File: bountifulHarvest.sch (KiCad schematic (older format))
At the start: 0 parts

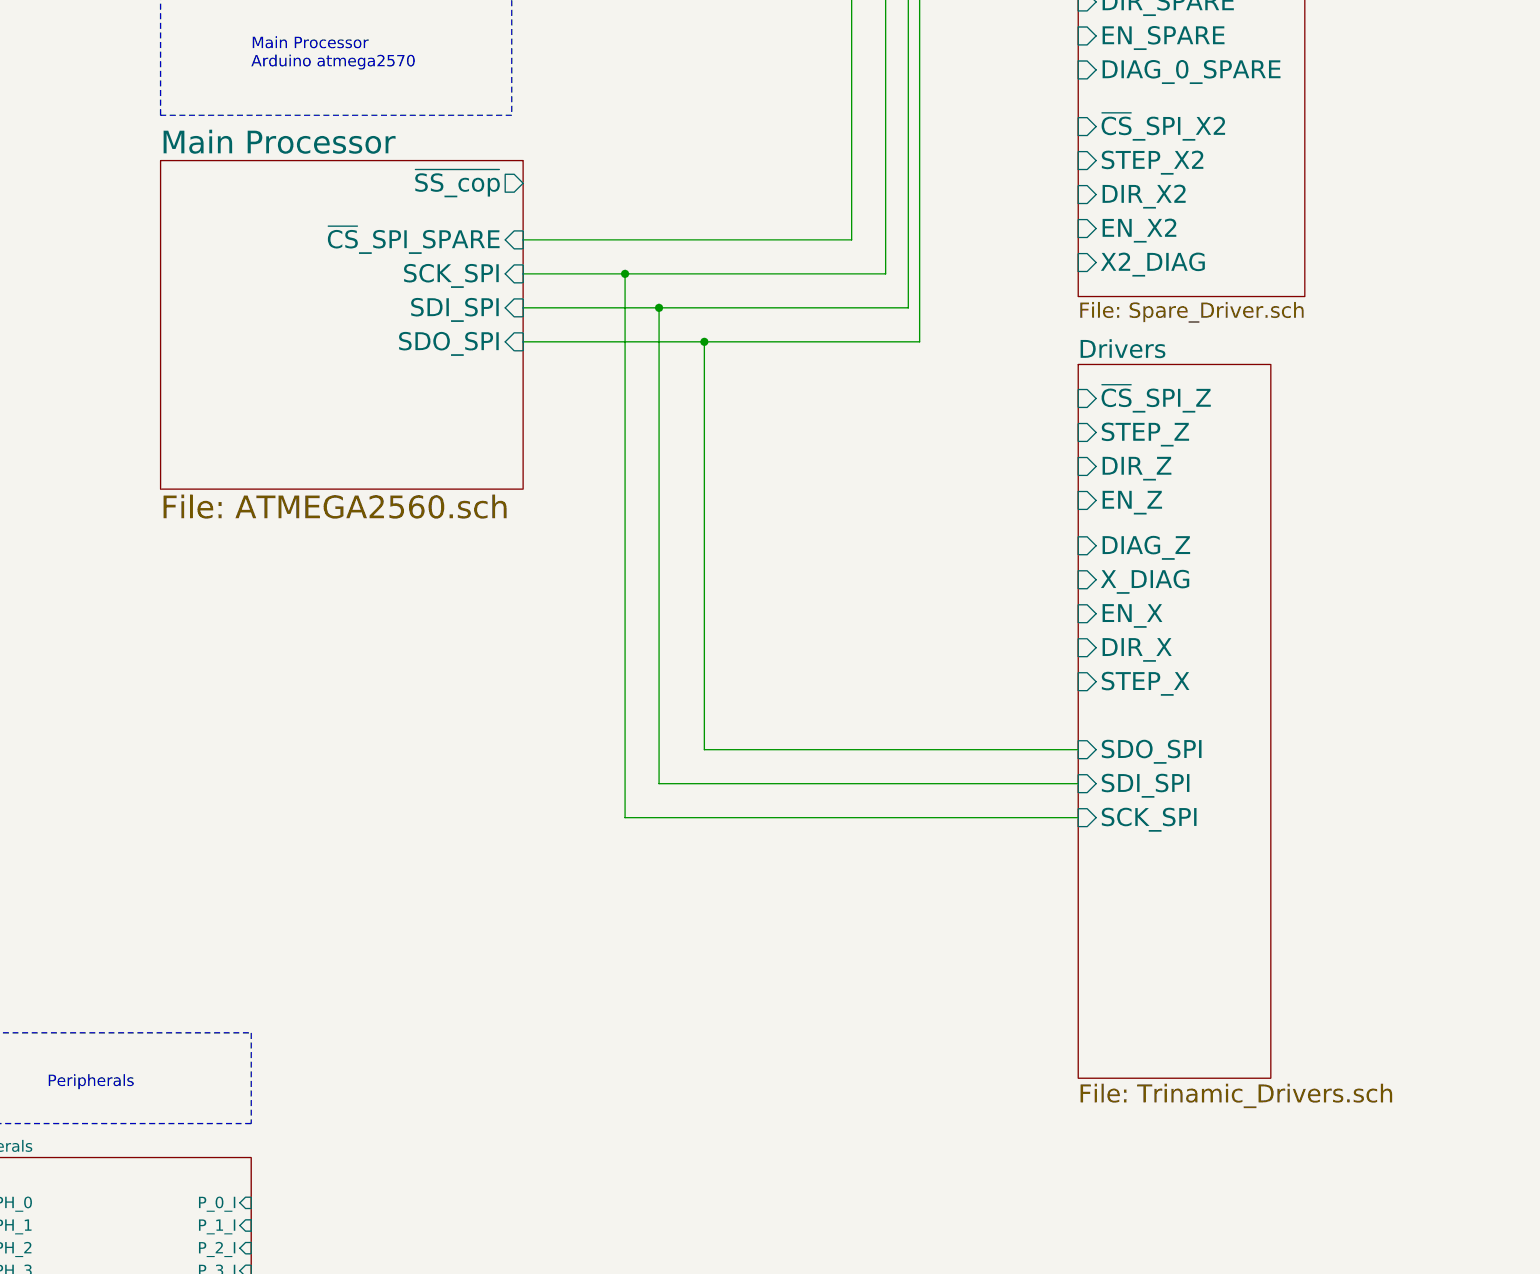
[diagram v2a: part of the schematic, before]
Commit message: Updated bus connections between drivers at ATMega
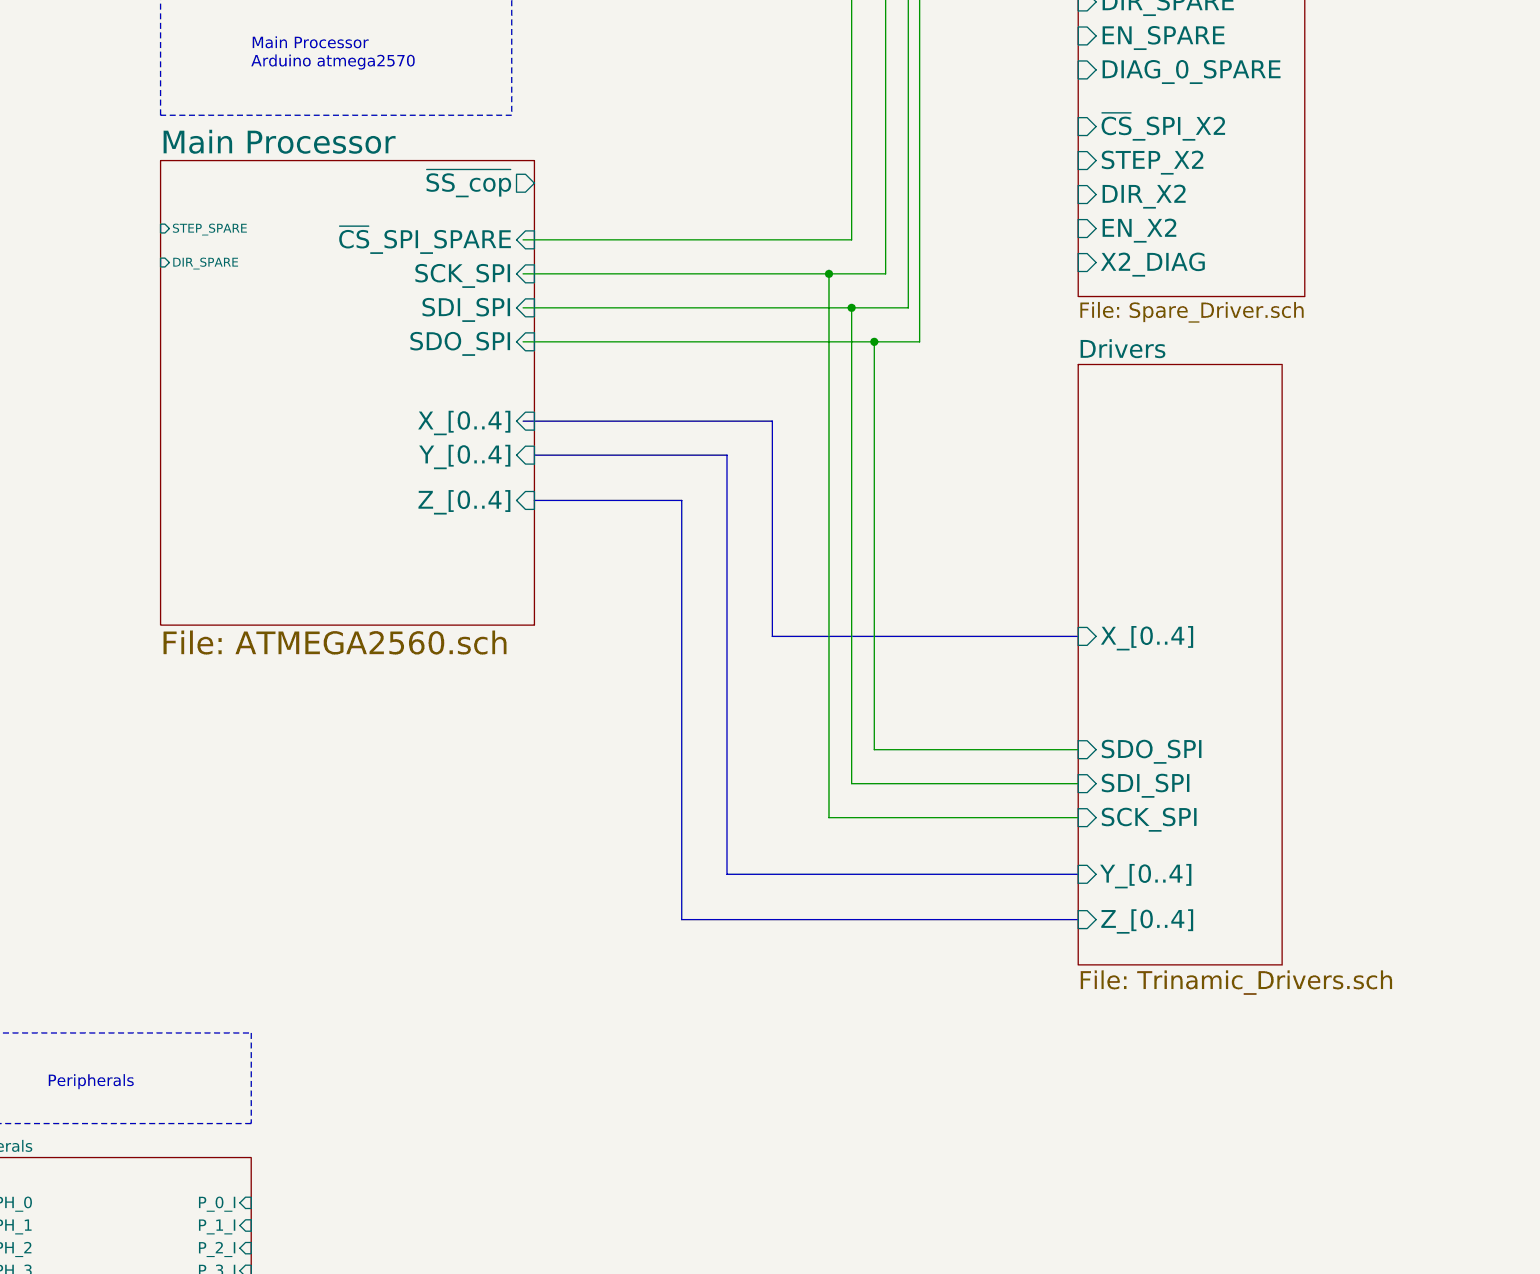
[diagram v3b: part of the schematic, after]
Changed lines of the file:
@@
 EESchema Schematic File Version 4
-EELAYER 30 0
+LIBS:bountifulHarvest-cache
+EELAYER 26 0
 EELAYER END
 $Descr A4 11693 8268
@@
 	6450 6150 6450 6550
 $Sheet
-S 10100 3200 850  3150
+S 6050 2300 1650 2050
+U 5EE66603
+F0 "Main Processor" 100
+F1 "ATMEGA2560.sch" 100
+F2 "~SS_cop" O R 7700 2400 79
+F3 "~CS~_SPI_SPARE" I R 7700 2650 79
+F4 "SCK_SPI" I R 7700 2800 79
+F5 "SDI_SPI" I R 7700 2950 79
+F6 "SDO_SPI" I R 7700 3100 79
+F7 "STEP_SPARE" I L 6050 2600 39
+F8 "DIR_SPARE" I L 6050 2750 39
+F9 "X_[0..4]" I R 7700 3450 79
+F10 "Y_[0..4]" I R 7700 3600 79
+F11 "Z_[0..4]" I R 7700 3800 79
+$EndSheet
+Wire Wire Line
+	7650 2650 9100 2650
+Wire Wire Line
+	9100 2650 9100 800
+Wire Wire Line
+	9100 800  10100 800
+Wire Wire Line
+	10100 950  9250 950
+Wire Wire Line
+	9250 950  9250 2800
+Wire Wire Line
+	9250 2800 9000 2800
+Wire Wire Line
+	10100 1100 9350 1100
+Wire Wire Line
+	9350 1100 9350 2950
+Wire Wire Line
+	9350 2950 9100 2950
+Wire Wire Line
+	7650 3100 9200 3100
+Wire Wire Line
+	9400 3100 9400 1250
+Wire Wire Line
+	9400 1250 10100 1250
+Wire Wire Line
+	10100 5200 9000 5200
+Wire Wire Line
+	9000 5200 9000 2800
+Connection ~ 9000 2800
+Wire Wire Line
+	9000 2800 7650 2800
+Wire Wire Line
+	10100 5050 9100 5050
+Wire Wire Line
+	9100 5050 9100 2950
+Connection ~ 9100 2950
+Wire Wire Line
+	9100 2950 7650 2950
+Wire Wire Line
+	10100 4900 9200 4900
+Wire Wire Line
+	9200 4900 9200 3100
+Connection ~ 9200 3100
+Wire Wire Line
+	9200 3100 9400 3100
+Wire Bus Line
+	10100 4400 8750 4400
+Wire Bus Line
+	8750 4400 8750 3450
+Wire Bus Line
+	8750 3450 7650 3450
+Wire Bus Line
+	10100 5450 8550 5450
+Wire Bus Line
+	8550 5450 8550 3600
+Wire Bus Line
+	8550 3600 7700 3600
+Wire Bus Line
+	10100 5650 8350 5650
+Wire Bus Line
+	8350 5650 8350 3800
+Wire Bus Line
+	8350 3800 7700 3800
+$Sheet
+S 10100 3200 900  2650
 U 5FF92876
 F0 "Drivers" 79
 F1 "Trinamic_Drivers.sch" 79
-F2 "~CS~_SPI_Z" I L 10100 3350 79
-F3 "STEP_Z" I L 10100 3500 79
-F4 "DIR_Z" I L 10100 3650 79
-F5 "EN_Z" I L 10100 3800 79
-F6 "DIAG_Z" I L 10100 4000 79
-F7 "X_DIAG" I L 10100 4150 79
-F8 "EN_X" I L 10100 4300 79
-F9 "DIR_X" I L 10100 4450 79
-F10 "STEP_X" I L 10100 4600 79
-F11 "SDO_SPI" I L 10100 4900 79
-F12 "SDI_SPI" I L 10100 5050 79
-F13 "SCK_SPI" I L 10100 5200 79
-$EndSheet
-$Sheet
-S 6050 2300 1600 1450
-U 5EE66603
-F0 "Main Processor" 100
-F1 "ATMEGA2560.sch" 100
-F2 "~SS_cop" O R 7650 2400 79
-F3 "~CS~_SPI_SPARE" I R 7650 2650 79
-F4 "SCK_SPI" I R 7650 2800 79
-F5 "SDI_SPI" I R 7650 2950 79
-F6 "SDO_SPI" I R 7650 3100 79
-$EndSheet
-Wire Wire Line
-	7650 2650 9100 2650
-Wire Wire Line
-	9100 2650 9100 800
-Wire Wire Line
-	9100 800  10100 800
-Wire Wire Line
-	10100 950  9250 950
-Wire Wire Line
-	9250 950  9250 2800
-Wire Wire Line
-	9250 2800 8100 2800
-Wire Wire Line
-	10100 1100 9350 1100
-Wire Wire Line
-	9350 1100 9350 2950
-Wire Wire Line
-	9350 2950 8250 2950
-Wire Wire Line
-	7650 3100 8450 3100
-Wire Wire Line
-	9400 3100 9400 1250
-Wire Wire Line
-	9400 1250 10100 1250
-Wire Wire Line
-	10100 5200 8100 5200
-Wire Wire Line
-	8100 5200 8100 2800
-Connection ~ 8100 2800
-Wire Wire Line
-	8100 2800 7650 2800
-Wire Wire Line
-	10100 5050 8250 5050
-Wire Wire Line
-	8250 5050 8250 2950
-Connection ~ 8250 2950
-Wire Wire Line
-	8250 2950 7650 2950
-Wire Wire Line
-	10100 4900 8450 4900
-Wire Wire Line
-	8450 4900 8450 3100
-Connection ~ 8450 3100
-Wire Wire Line
-	8450 3100 9400 3100
+F2 "SDO_SPI" I L 10100 4900 79
+F3 "SDI_SPI" I L 10100 5050 79
+F4 "SCK_SPI" I L 10100 5200 79
+F5 "X_[0..4]" I L 10100 4400 79
+F6 "Y_[0..4]" I L 10100 5450 79
+F7 "Z_[0..4]" I L 10100 5650 79
+$EndSheet
 $EndSCHEMATC

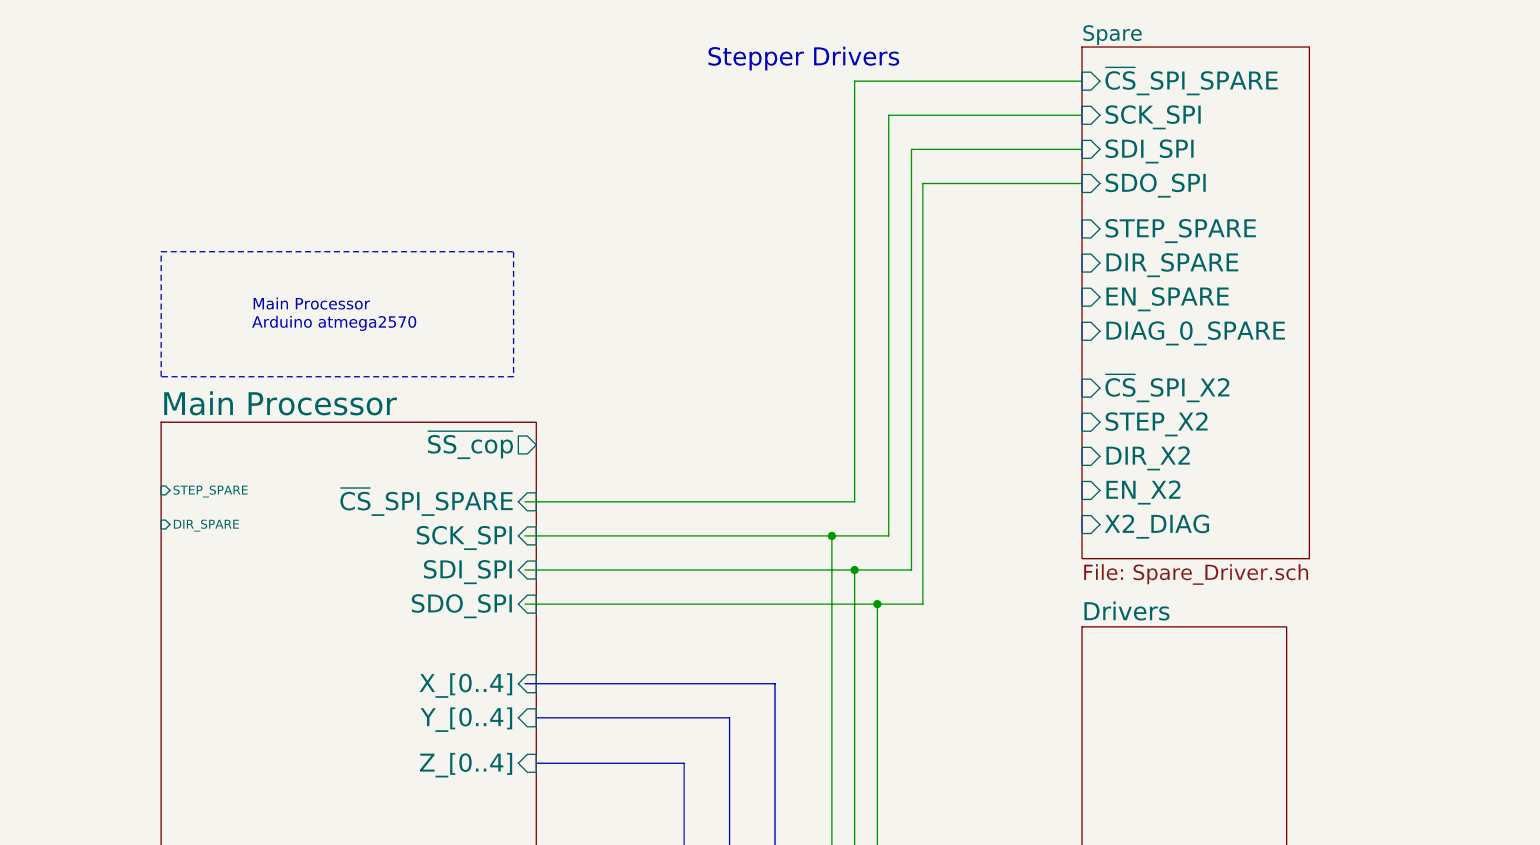
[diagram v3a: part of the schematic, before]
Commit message: Fixed X,Y,Z driver bus connection. set up spare and X2
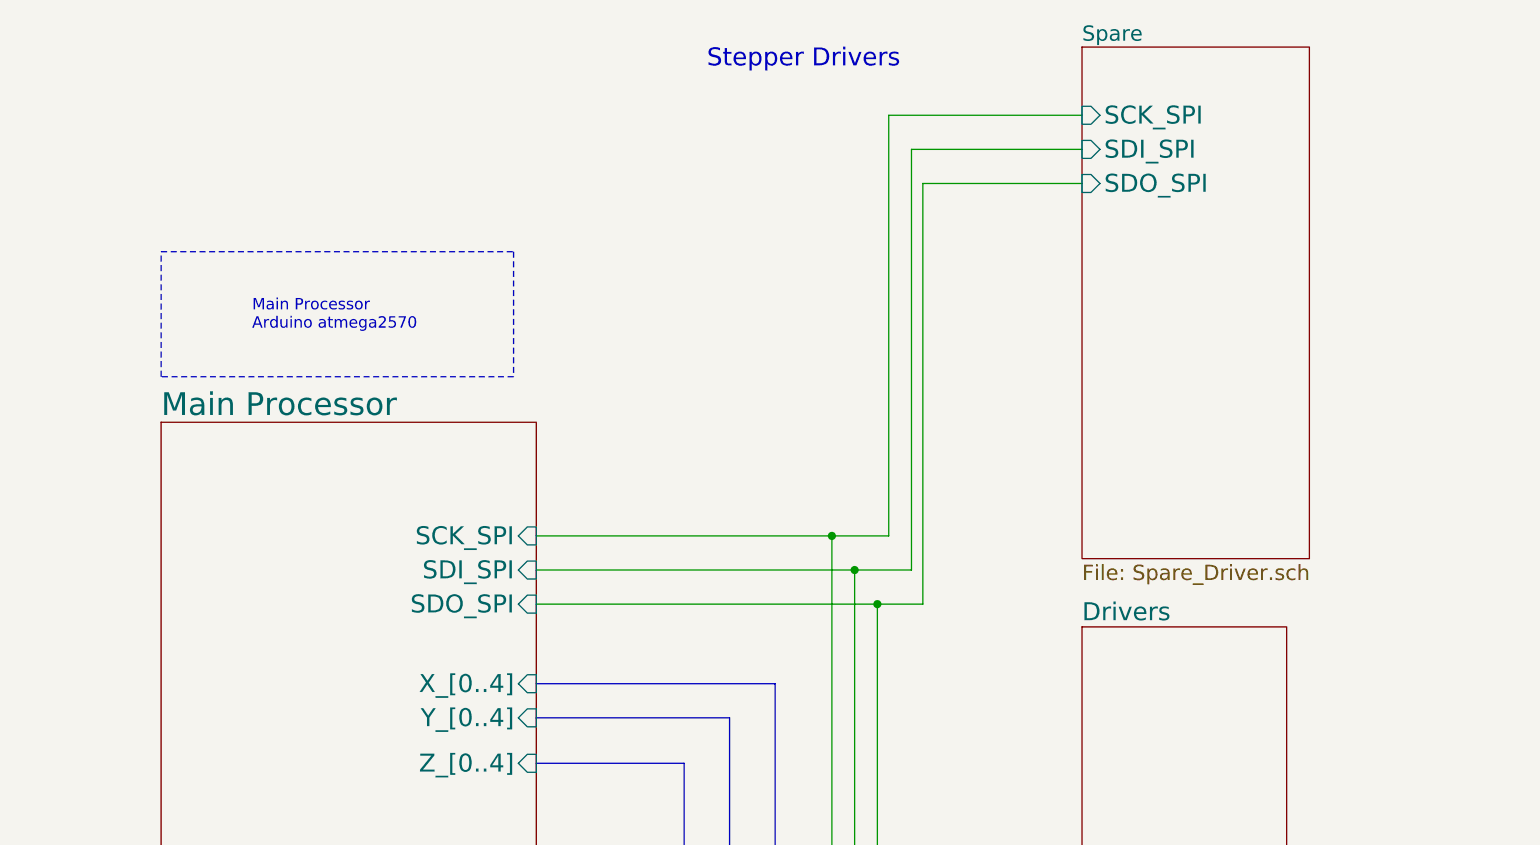
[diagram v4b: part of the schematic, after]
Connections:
- wire segments 21 -> 18
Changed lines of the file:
@@
 Stepper Drivers
-$Sheet
-S 10100 650  1000 2250
-U 5EEE69C6
-F0 "Spare" 67
-F1 "Spare_Driver.sch" 67
-F2 "~CS~_SPI_SPARE" I L 10100 800 79
-F3 "SCK_SPI" I L 10100 950 79
-F4 "SDI_SPI" I L 10100 1100 79
-F5 "SDO_SPI" I L 10100 1250 79
-F6 "STEP_SPARE" I L 10100 1450 79
-F7 "DIR_SPARE" I L 10100 1600 79
-F8 "EN_SPARE" I L 10100 1750 79
-F9 "~CS~_SPI_X2" I L 10100 2150 79
-F10 "STEP_X2" I L 10100 2300 79
-F11 "DIR_X2" I L 10100 2450 79
-F12 "EN_X2" I L 10100 2600 79
-F13 "X2_DIAG" I L 10100 2750 79
-F14 "DIAG_0_SPARE" I L 10100 1900 79
-$EndSheet
 $Sheet
 S 5100 6700 1350 700
@@
 F0 "Main Processor" 100
 F1 "ATMEGA2560.sch" 100
-F2 "~SS_cop" O R 7700 2400 79
-F3 "~CS~_SPI_SPARE" I R 7700 2650 79
-F4 "SCK_SPI" I R 7700 2800 79
-F5 "SDI_SPI" I R 7700 2950 79
-F6 "SDO_SPI" I R 7700 3100 79
-F7 "STEP_SPARE" I L 6050 2600 39
-F8 "DIR_SPARE" I L 6050 2750 39
-F9 "X_[0..4]" I R 7700 3450 79
-F10 "Y_[0..4]" I R 7700 3600 79
-F11 "Z_[0..4]" I R 7700 3800 79
+F2 "SCK_SPI" I R 7700 2800 79
+F3 "SDI_SPI" I R 7700 2950 79
+F4 "SDO_SPI" I R 7700 3100 79
+F5 "X_[0..4]" I R 7700 3450 79
+F6 "Y_[0..4]" I R 7700 3600 79
+F7 "Z_[0..4]" I R 7700 3800 79
 $EndSheet
-Wire Wire Line
-	7650 2650 9100 2650
-Wire Wire Line
-	9100 2650 9100 800
-Wire Wire Line
-	9100 800  10100 800
 Wire Wire Line
 	10100 950  9250 950
@@
 	9350 2950 9100 2950
 Wire Wire Line
-	7650 3100 9200 3100
+	7700 3100 9200 3100
 Wire Wire Line
 	9400 3100 9400 1250
@@
 Connection ~ 9000 2800
 Wire Wire Line
-	9000 2800 7650 2800
+	9000 2800 7700 2800
 Wire Wire Line
 	10100 5050 9100 5050
@@
 Connection ~ 9100 2950
 Wire Wire Line
-	9100 2950 7650 2950
+	9100 2950 7700 2950
 Wire Wire Line
 	10100 4900 9200 4900
@@
 Wire Bus Line
 	8750 4400 8750 3450
-Wire Bus Line
-	8750 3450 7650 3450
 Wire Bus Line
 	10100 5450 8550 5450
@@
 F7 "Z_[0..4]" I L 10100 5650 79
 $EndSheet
+Wire Bus Line
+	7700 3450 8750 3450
+$Sheet
+S 10100 650  1000 2250
+U 5EEE69C6
+F0 "Spare" 67
+F1 "Spare_Driver.sch" 67
+F2 "SCK_SPI" I L 10100 950 79
+F3 "SDI_SPI" I L 10100 1100 79
+F4 "SDO_SPI" I L 10100 1250 79
+$EndSheet
 $EndSCHEMATC

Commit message: added peripherals
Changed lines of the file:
@@
 $EndSheet
 Wire Notes Line
-	5100 6150 6450 6150
+	4300 5900 5650 5900
 Wire Notes Line
 	1000 4200 2100 4200
@@
 Stepper Drivers
 $Sheet
-S 5100 6700 1350 700
+S 4350 6450 1350 700
 U 5F08C095
 F0 "peripherals" 50
 F1 "FET_drivers.sch" 50
-F2 "PERIPH_0" I L 5100 6900 50
-F3 "PERIPH_1" I L 5100 7000 50
-F4 "PERIPH_2" I L 5100 7100 50
-F5 "PERIPH_3" I L 5100 7200 50
-F6 "P_0_I" I R 6450 6900 50
-F7 "P_3_I" I R 6450 7200 50
-F8 "P_1_I" I R 6450 7000 50
-F9 "P_2_I" I R 6450 7100 50
+F2 "PERIPH_0" I R 5700 6650 50
+F3 "PERIPH_1" I R 5700 6750 50
+F4 "PERIPH_2" I R 5700 6850 50
+F5 "PERIPH_3" I R 5700 6950 50
+F6 "P_0_I" I L 4350 6650 50
+F7 "P_3_I" I L 4350 6950 50
+F8 "P_1_I" I L 4350 6750 50
+F9 "P_2_I" I L 4350 6850 50
 $EndSheet
-Text Notes 5550 6400 0    50   ~ 0
+Text Notes 4750 6150 0    50   ~ 0
 Peripherals\n
 Wire Notes Line
-	5100 6550 5100 6150
+	4300 6300 4300 5900
 Wire Notes Line
-	6450 6550 5100 6550
+	5650 6300 4300 6300
 Wire Notes Line
-	6450 6150 6450 6550
+	5650 5900 5650 6300
 $Sheet
-S 6050 2300 1650 2050
+S 6050 2300 1650 3000
 U 5EE66603
 F0 "Main Processor" 100
@@
 F6 "Y_[0..4]" I R 7700 3600 79
 F7 "Z_[0..4]" I R 7700 3800 79
+F8 "~SS_cop" O L 6050 2800 39
+F9 "X2_[0..4]" I R 7700 3300 79
+F10 "P_0_I" I L 6050 5000 59
+F11 "P_1_I" I L 6050 4850 59
+F12 "P_2_I" I L 6050 4700 59
+F13 "P_3_I" I L 6050 4550 59
 $EndSheet
 Wire Wire Line
@@
 	9400 1250 10100 1250
 Wire Wire Line
-	10100 5200 9000 5200
+	10100 4550 9000 4550
 Wire Wire Line
-	9000 5200 9000 2800
+	9000 4550 9000 2800
 Connection ~ 9000 2800
 Wire Wire Line
 	9000 2800 7700 2800
 Wire Wire Line
-	10100 5050 9100 5050
+	10100 4400 9100 4400
 Wire Wire Line
-	9100 5050 9100 2950
+	9100 4400 9100 2950
 Connection ~ 9100 2950
 Wire Wire Line
 	9100 2950 7700 2950
 Wire Wire Line
-	10100 4900 9200 4900
+	10100 4250 9200 4250
 Wire Wire Line
-	9200 4900 9200 3100
+	9200 4250 9200 3100
 Connection ~ 9200 3100
 Wire Wire Line
 	9200 3100 9400 3100
 Wire Bus Line
-	10100 4400 8750 4400
+	10100 5300 8900 5300
 Wire Bus Line
-	8750 4400 8750 3450
+	8900 5300 8900 3450
 Wire Bus Line
-	10100 5450 8550 5450
+	10100 5450 8800 5450
 Wire Bus Line
-	8550 5450 8550 3600
+	8800 5450 8800 3600
 Wire Bus Line
-	8550 3600 7700 3600
+	8800 3600 7700 3600
 Wire Bus Line
-	10100 5650 8350 5650
+	10100 5650 8750 5650
 Wire Bus Line
-	8350 5650 8350 3800
+	8750 5650 8750 3800
 Wire Bus Line
-	8350 3800 7700 3800
+	8750 3800 7700 3800
 $Sheet
 S 10100 3200 900  2650
@@
 F0 "Drivers" 79
 F1 "Trinamic_Drivers.sch" 79
-F2 "SDO_SPI" I L 10100 4900 79
-F3 "SDI_SPI" I L 10100 5050 79
-F4 "SCK_SPI" I L 10100 5200 79
-F5 "X_[0..4]" I L 10100 4400 79
+F2 "SDO_SPI" I L 10100 4250 79
+F3 "SDI_SPI" I L 10100 4400 79
+F4 "SCK_SPI" I L 10100 4550 79
+F5 "X_[0..4]" I L 10100 5300 79
 F6 "Y_[0..4]" I L 10100 5450 79
 F7 "Z_[0..4]" I L 10100 5650 79
 $EndSheet
 Wire Bus Line
-	7700 3450 8750 3450
+	7700 3450 8900 3450
 $Sheet
 S 10100 650  1000 2250
@@
 F3 "SDI_SPI" I L 10100 1100 79
 F4 "SDO_SPI" I L 10100 1250 79
+F5 "X2_[0..4]" I L 10100 1800 79
 $EndSheet
+Wire Bus Line
+	9550 3300 9550 1800
+Wire Bus Line
+	9550 1800 10100 1800
+Wire Bus Line
+	7700 3300 9550 3300
+Wire Wire Line
+	6050 5000 4150 5000
+Wire Wire Line
+	4150 5000 4150 6650
+Wire Wire Line
+	4150 6650 4350 6650
+Wire Wire Line
+	4350 6750 4000 6750
+Wire Wire Line
+	4000 6750 4000 4850
+Wire Wire Line
+	4000 4850 6050 4850
+Wire Wire Line
+	6050 4700 3900 4700
+Wire Wire Line
+	3900 4700 3900 6850
+Wire Wire Line
+	3900 6850 4350 6850
+Wire Wire Line
+	6050 4550 3850 4550
+Wire Wire Line
+	3850 4550 3850 6950
+Wire Wire Line
+	3850 6950 4350 6950
 $EndSCHEMATC
